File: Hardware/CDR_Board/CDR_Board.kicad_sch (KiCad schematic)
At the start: 62 parts, among them J1 nRF52, J2 nRF24, J3 Battery, J4 GPIO & ADC, J5 USB_C_Receptacle_USB2.0, Q1 DMP2045U, SW1 BOOTSEL, SW2 RESET, SW3 SW_SPDT, U1 W25Q32JVSS, U2 AP2112, U3 RP2040, U4 BQ25172, U6 ADXL343, Y1 Crystal

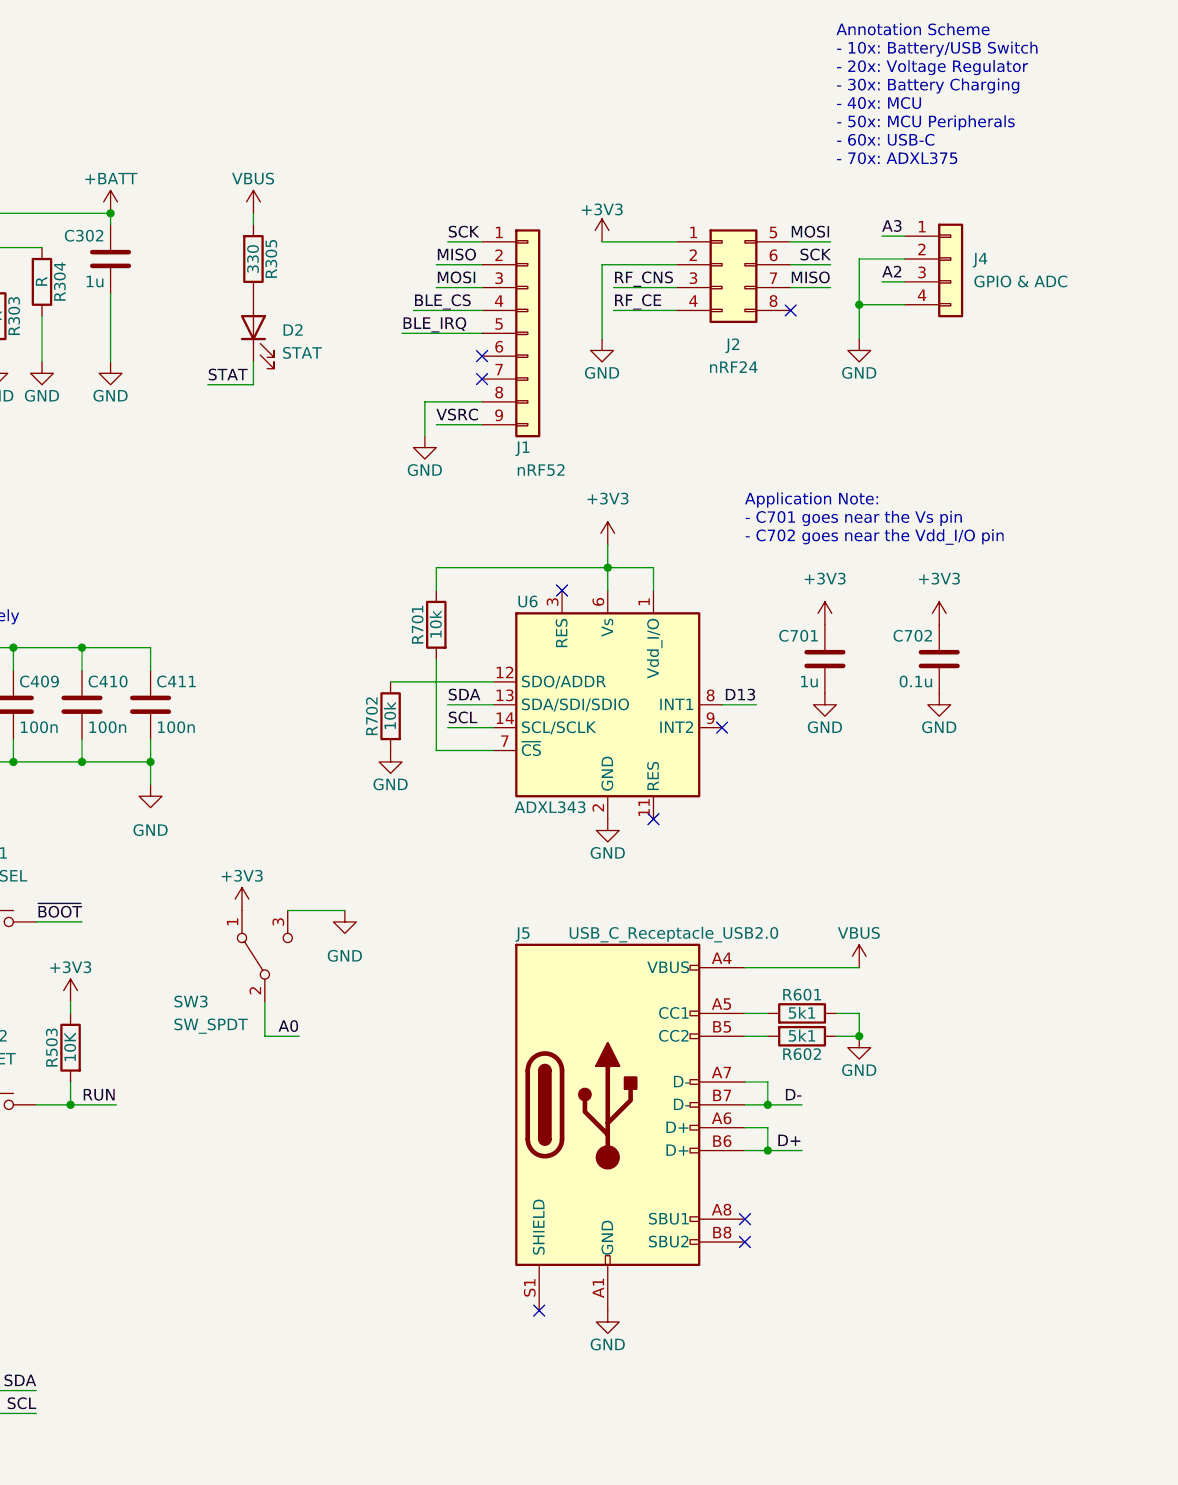
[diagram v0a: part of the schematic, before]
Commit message: Updated helmet PCB
Added voltage divider for battery measurement, pull-down resistor for FSR measurement
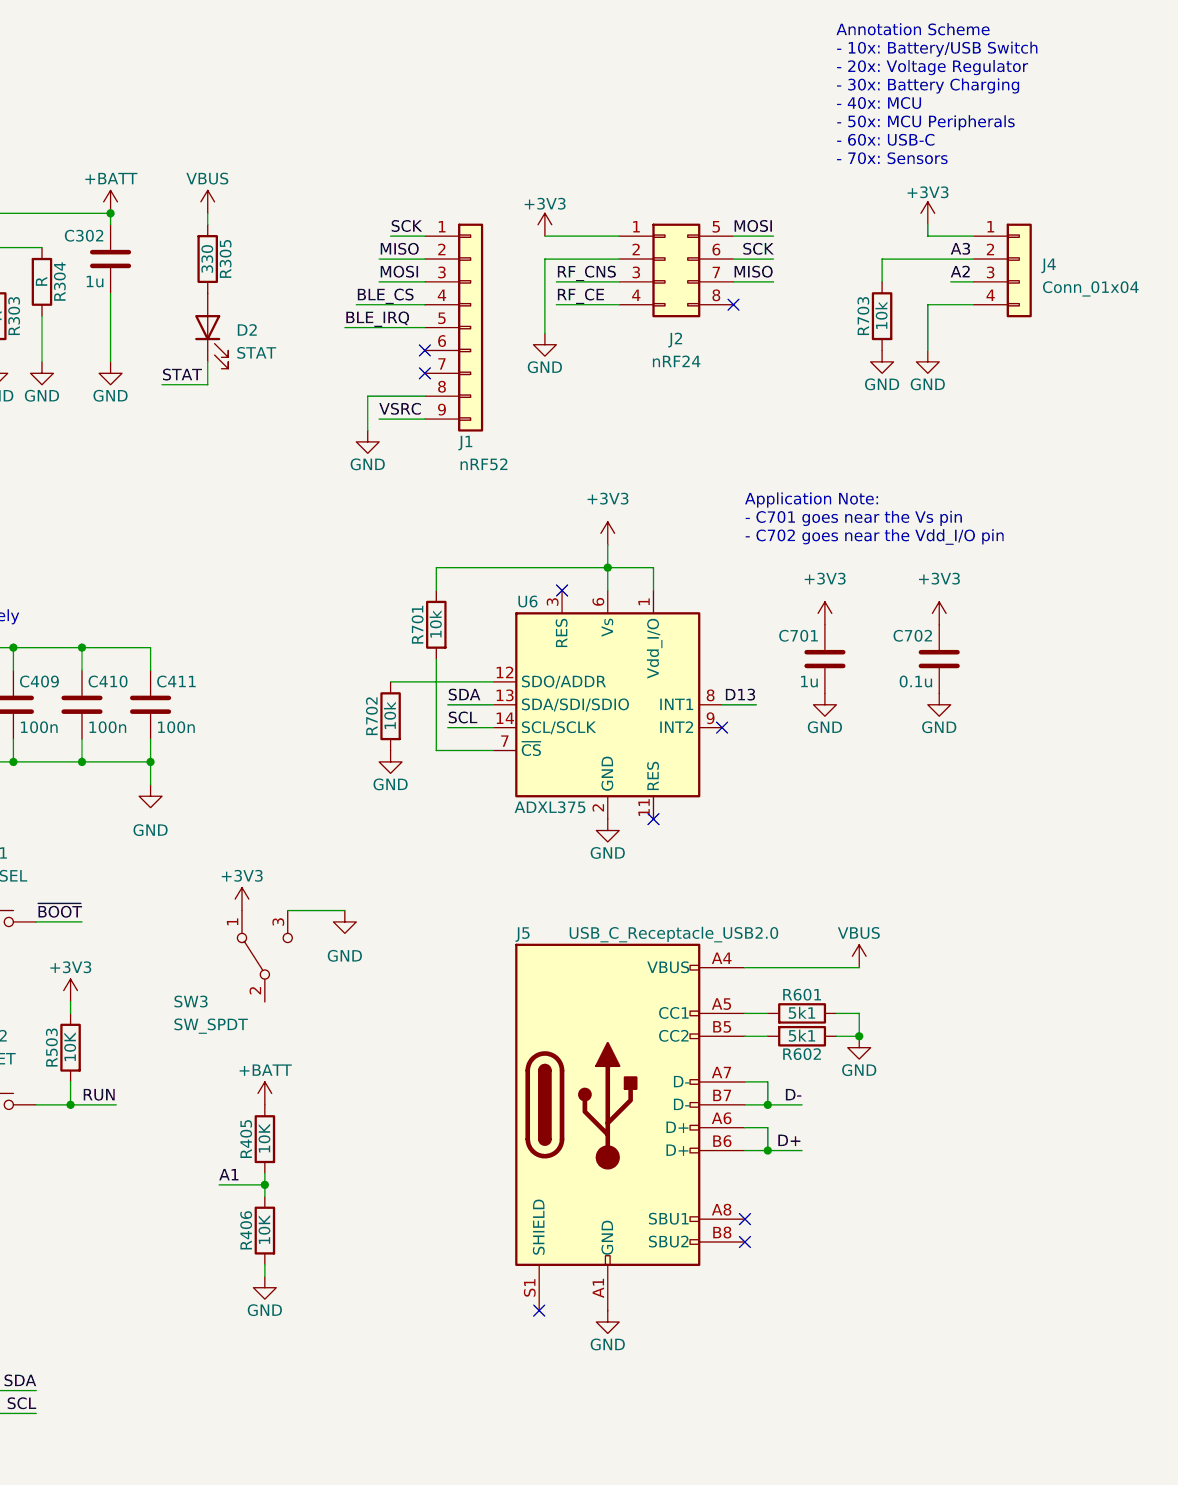
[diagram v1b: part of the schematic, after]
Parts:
- added R405, R406: 10K, Resistor_SMD:R_0805_2012Metric_Pad1.20x1.40mm_HandSolder, symbol Device:R
- added R703: 10k, Resistor_SMD:R_0805_2012Metric_Pad1.20x1.40mm_HandSolder, symbol Device:R
- J4: value GPIO & ADC -> Conn_01x04
- U6: value ADXL343 -> ADXL375
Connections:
- net +3V3: now also J4.1 (Pin_1)
- net +BATT: now also R405.1
- net A0: no longer SW3.2 (B)
- net A1: now also R405.2, R406.1
- net A3: now also J4.2 (Pin_2), R703.1; no longer J4.1 (Pin_1)
- net GND: now also R406.2, R703.2; no longer J4.2 (Pin_2)
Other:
- note added: "Annotation Scheme - 10x: Battery/USB Switch - 20x: Voltage Regulator - 30x: Battery Charging - 40x: MCU - 50x: MCU Peripherals - 60x: USB-C - 70x: Sensors"
- note removed: "Annotation Scheme - 10x: Battery/USB Switch - 20x: Voltage Regulator - 30x: Battery Charging - 40x: MCU - 50x: MCU Peripherals - 60x: USB-C - 70x: ADXL375"
- moved on the sheet: D2, J1, J2, R305

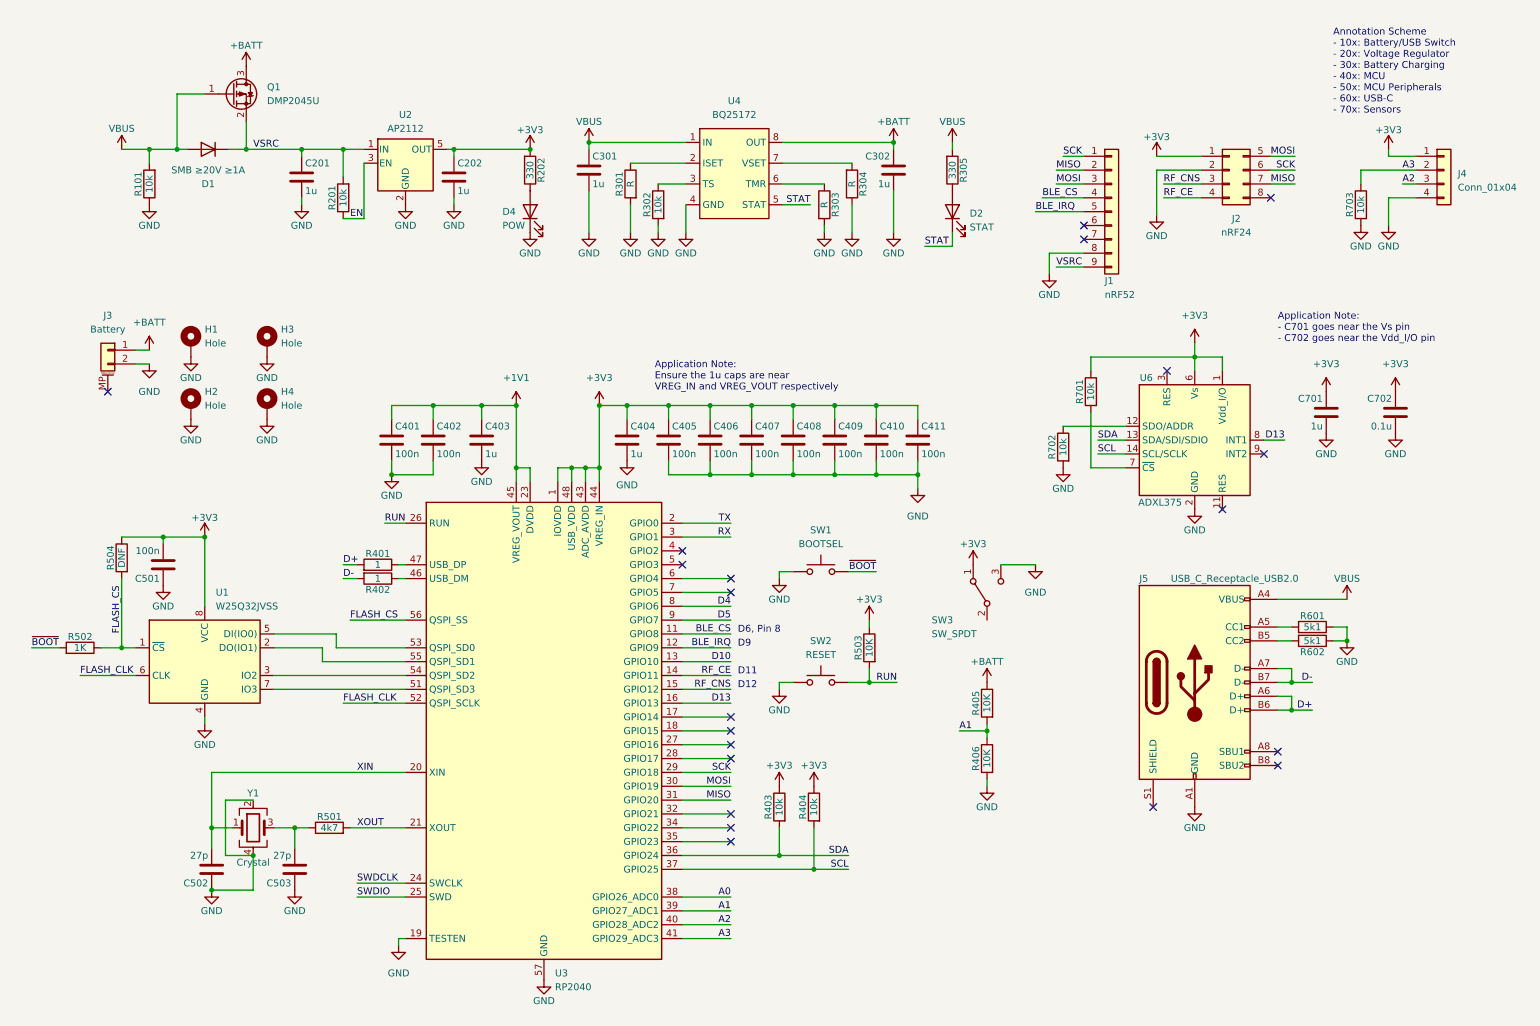
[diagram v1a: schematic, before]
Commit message: Updated ADXL375 I2C, helmet PCB
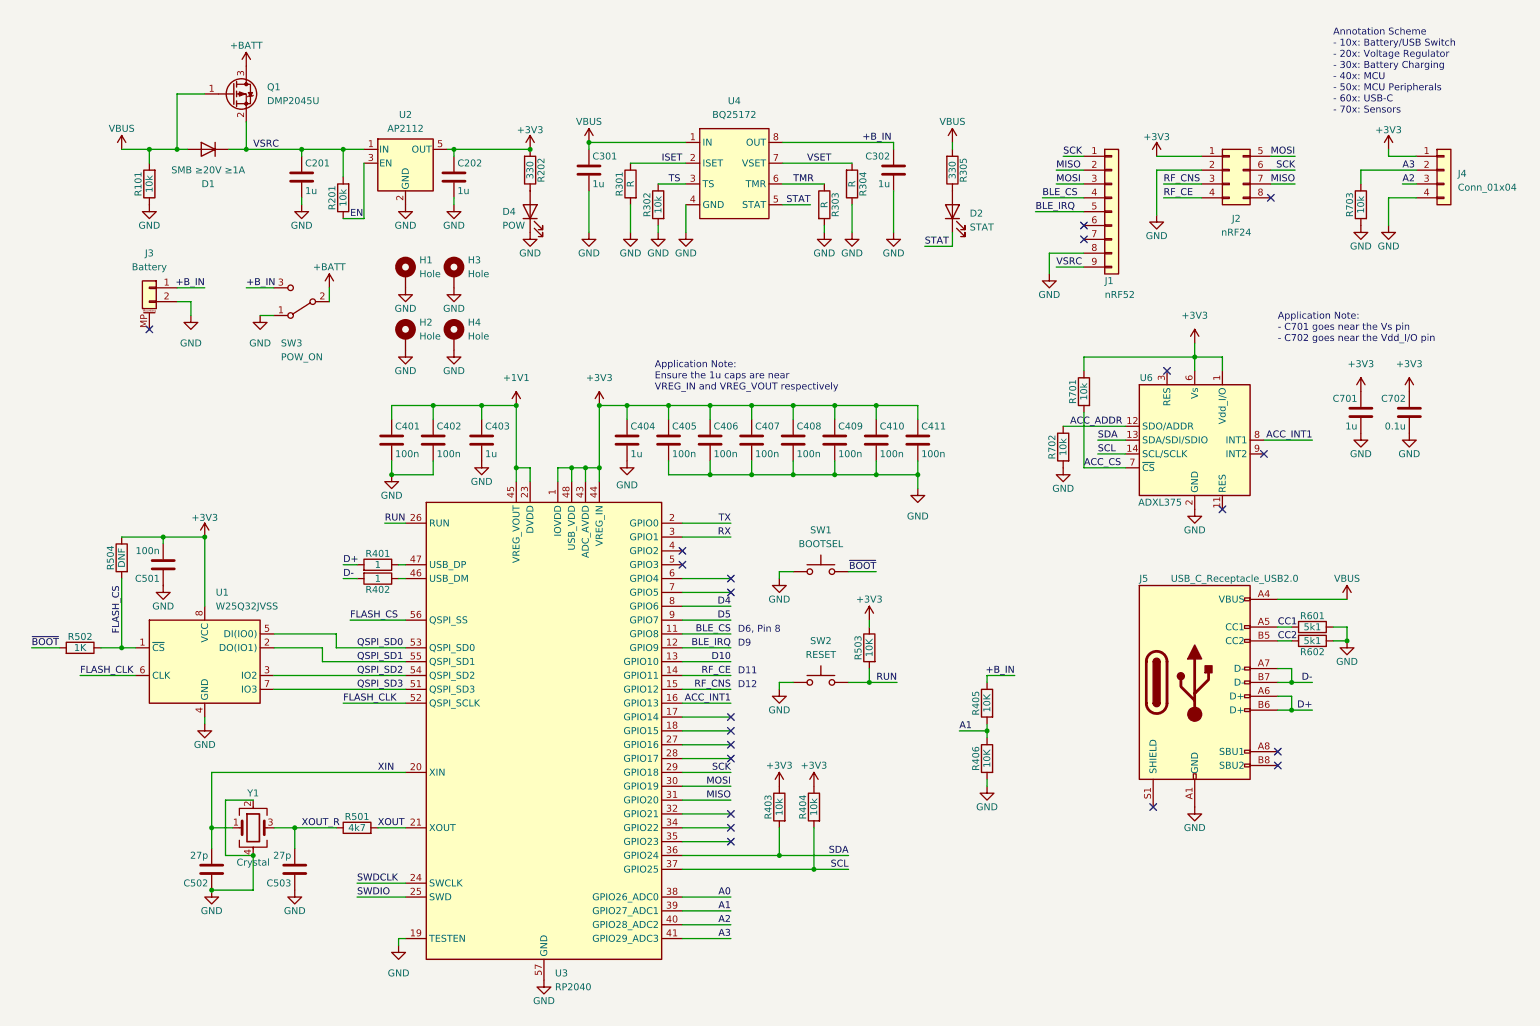
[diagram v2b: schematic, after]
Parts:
- SW3: value SW_SPDT -> POW_ON
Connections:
- net +3V3: no longer SW3.1 (A)
- net +BATT: now also SW3.2 (B); no longer C302.1, J3.1 (Pin_1), R405.1, U4.8 (OUT)
- net GND: now also SW3.1 (A); no longer SW3.3 (C)
- net QSPI_SD3: now reaches U1.7 (IO3), U3.51 (QSPI_SD3)
- net QSPI_SD0: now reaches U1.5 (DI(IO0)), U3.53 (QSPI_SD0)
- net QSPI_SD2: now reaches U1.3 (IO2), U3.54 (QSPI_SD2)
- net QSPI_SD1: now reaches U1.2 (DO(IO1)), U3.55 (QSPI_SD1)
- net CC1: now reaches J5.A5 (CC1), R601.2
- net CC2: now reaches J5.B5 (CC2), R602.2
- net XOUT_R: now reaches C503.2, R501.1, Y1.3
- net TMR: now reaches R303.1, U4.6 (TMR)
- net ACC_CS: now reaches R701.2, U6.7 (~{CS})
- net VSET: now reaches R304.2, U4.7 (VSET)
- net ISET: now reaches R301.1, U4.2 (ISET)
- net TS: now reaches R302.1, U4.3 (TS)
- net ACC_ADDR: now reaches R702.1, U6.12 (SDO/ADDR)
- net D13 renamed ACC_INT1
- new net +B_IN: C302.1, J3.1 (Pin_1), R405.1, SW3.3 (C), U4.8 (OUT)
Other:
- moved on the sheet: C701, C702, H1, H2, H3, H4, J3, R501, R701, SW3

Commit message: FPR System Software
Finished software for FPR helmet
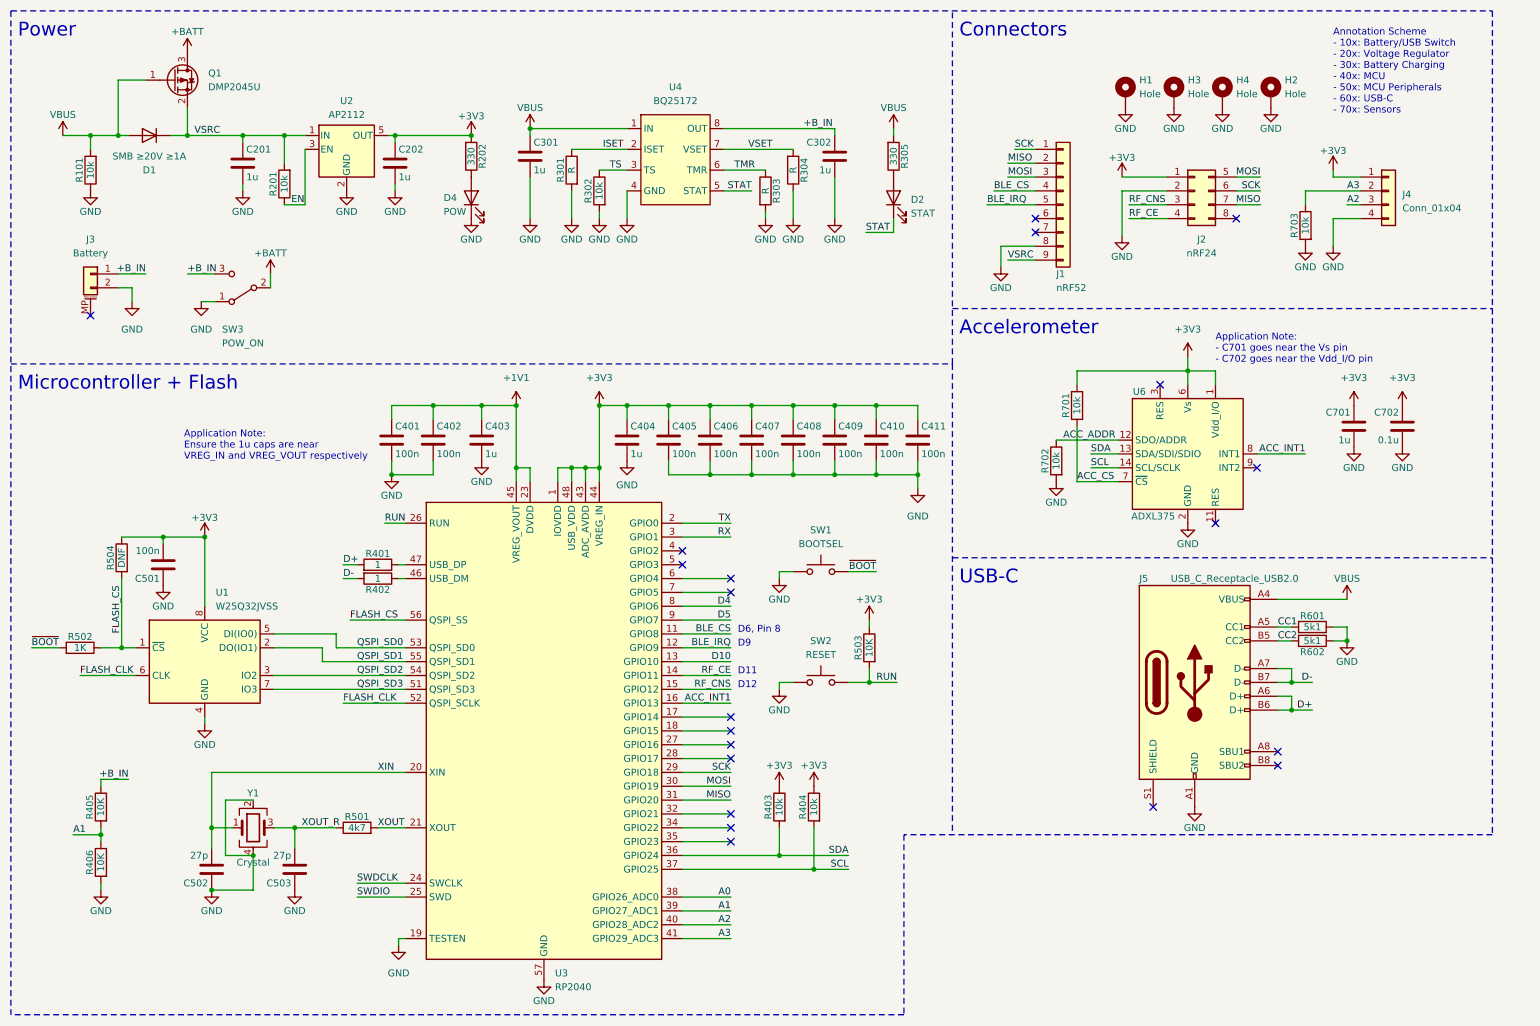
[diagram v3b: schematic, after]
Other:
- note added: "Accelerometer"
- note added: "Connectors"
- note added: "Microcontroller + Flash"
- note added: "Power"
- note added: "USB-C"
- moved on the sheet: C201, C202, C301, C302, C701, C702, D1, D2, D4, H1, H2, H3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
